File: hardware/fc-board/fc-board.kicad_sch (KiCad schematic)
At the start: 0 parts

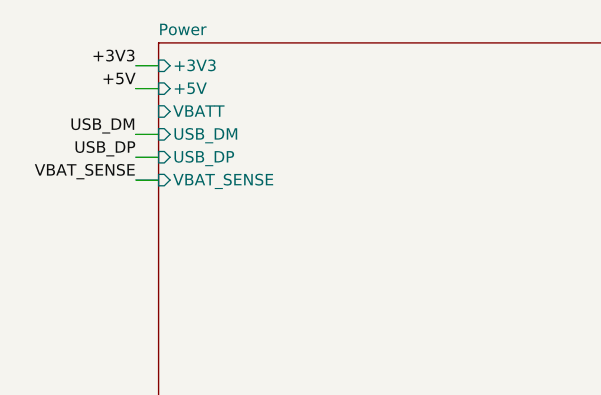
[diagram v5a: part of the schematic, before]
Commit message: Remove external footprint dependency; make VBATT sheet-local
R1-R7 repointed from SparkFun-Resistor to Resistor_SMD:R_0603_1608Metric, the stock KiCad footprint already used by R20-R26 -- identical 0603 land pattern, so a clean checkout no longer needs a library it does not have. VBATT demoted from hierarchical to local label on the power sheet and its orphaned root-sheet pin removed: the net is consumed entirely on the power sheet by the sense divider, so exporting it created a sheet pin with no consumer and the project's only ERC violation. ERC now clean.
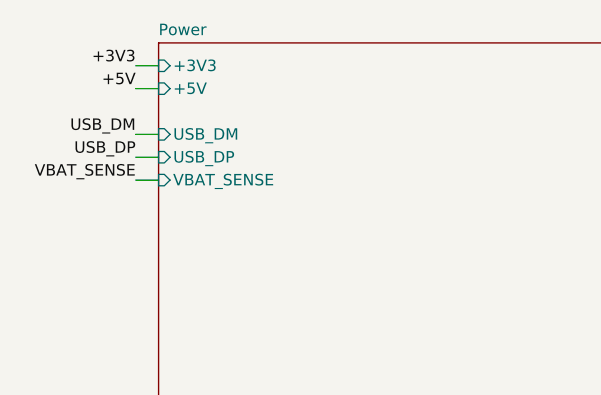
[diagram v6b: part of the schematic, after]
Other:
- sheet Power ports: added none; removed VBATT
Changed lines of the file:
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@@
-			)
-		)
-		(pin "VBATT" input
-			(at 15.24 24.13 180)
-			(effects
-				(font
-					(size 1.27 1.27)
-				)
-				(justify left)
 			)
 		)
